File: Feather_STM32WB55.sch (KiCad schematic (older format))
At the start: 45 parts, among them J1 JST-SH Qwiic, J2 Conn_Battery, J3 Conn_ARM_JTAG_SWD_10, J4 Conn_Right, J5 USB_C_Receptacle_USB2.0, J6 Conn_Left, Q1 NTR4171PT1G, SW1 SMD-BUTTON-TOP-DHT-4235A_4P-4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, U1 MCP73831-2-OT, U2 AP2112K-3.3, U3 STM32WB55CGU6, U4 USBLC6-2SC6, U5 Flash SOIC-8, Y1 32Mhz

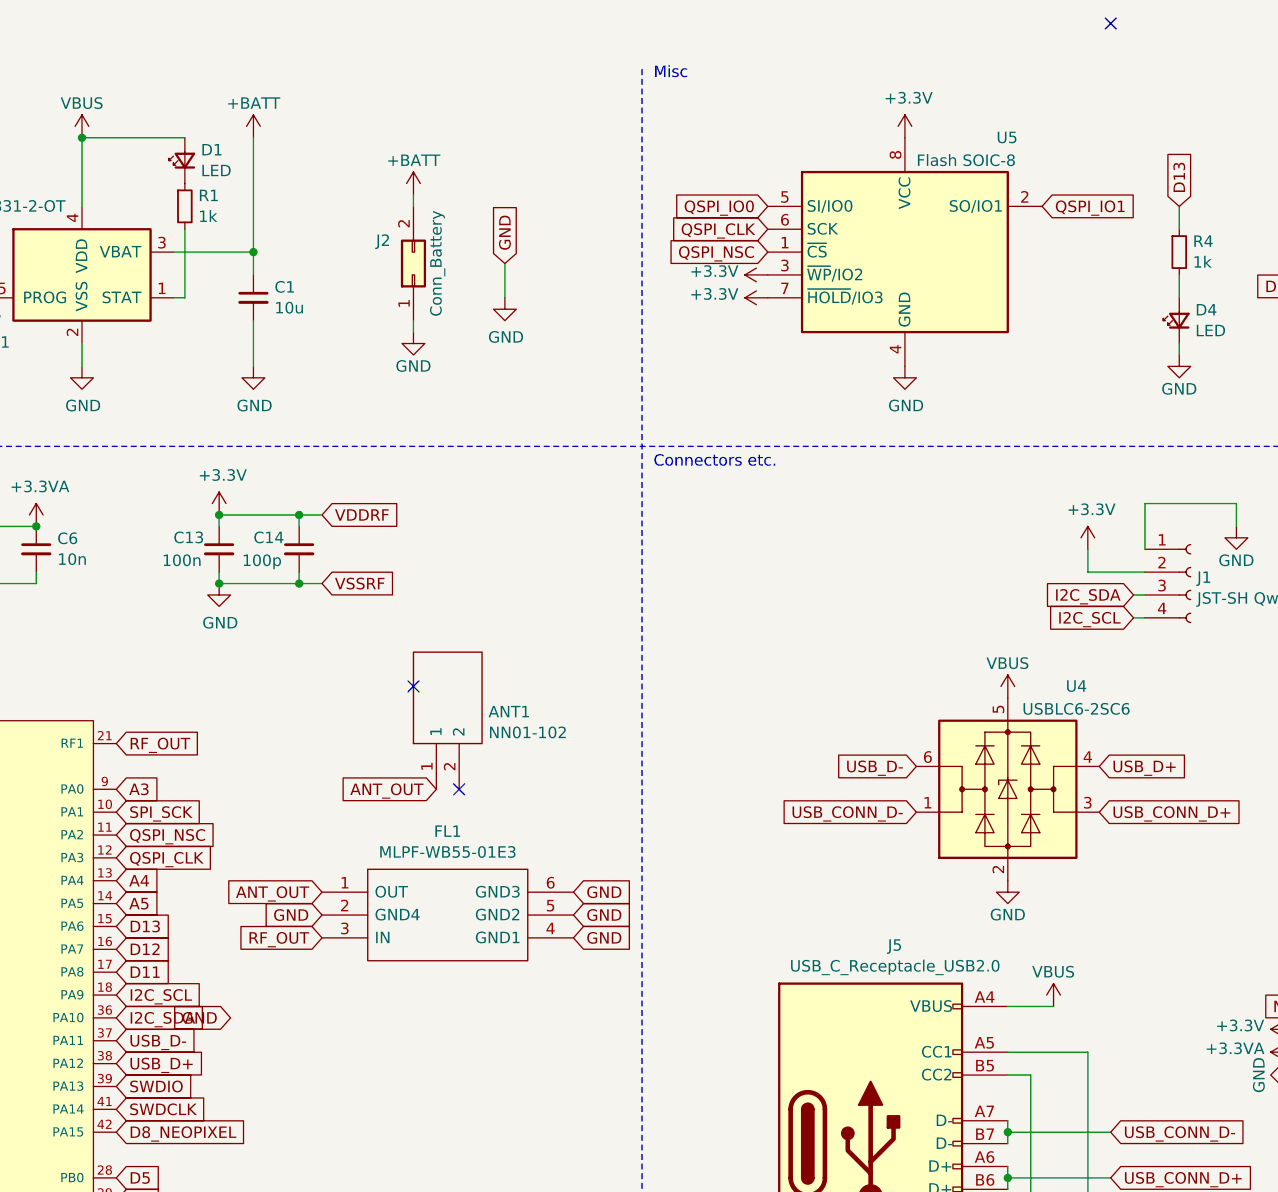
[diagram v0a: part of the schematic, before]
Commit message: fix: repair STM32WB55 short and restore project libraries (#1)
* docs: improve project discovery and reuse guidance

Describe the historical design and available artifacts from repository evidence. Keep hardware and fabrication outputs unchanged, preserve third-party rights, and make unresolved setup and validation limits visible.

* docs: record completed discoverability delivery

* fix: clear the D10 ground short and restore legacy libraries

Move the overlapping ground via using a controlled before/after zone-refilled DRC comparison. Recover original dependencies and align component identifiers without redesigning the land pattern or guessing the physical stackup. Keep historical fabrication outputs explicitly separate from corrected source.

* docs: record completed source audit delivery

* docs: qualify nightly netlist validation by library resolution

Independent export checks show nightly legacy global-library resolution omits the USB shield pin despite identical cached and global pin geometry. Document the exact cache-only invocation and retain the source without speculative wiring changes.
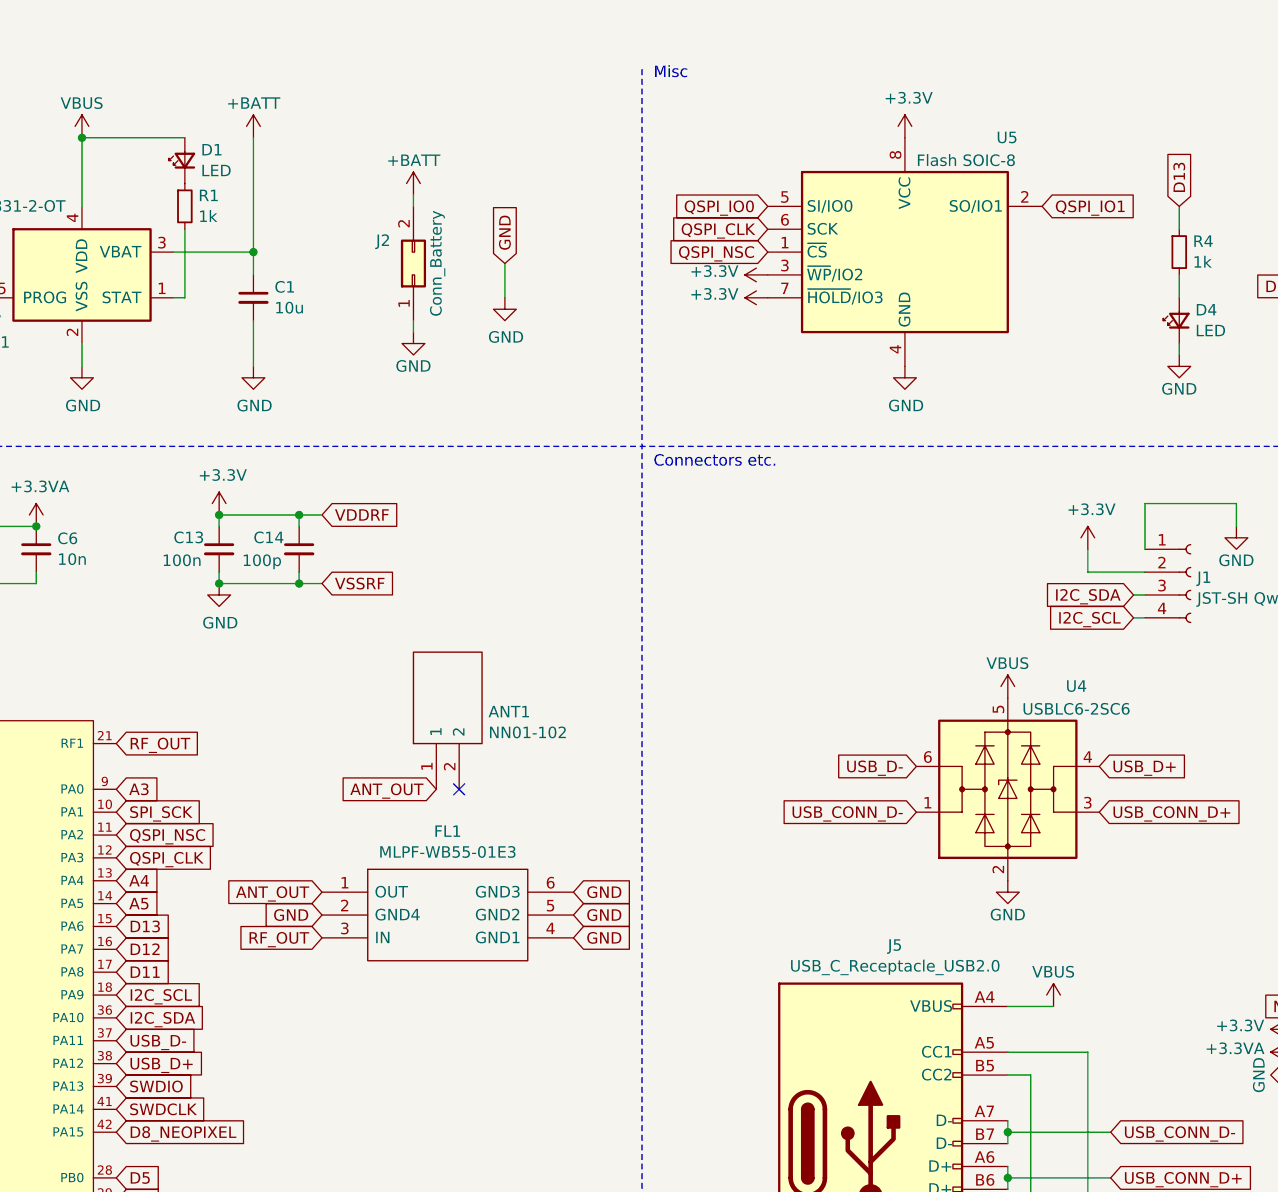
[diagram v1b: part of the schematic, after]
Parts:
- ANT1: footprint FR05S1N0102 -> Makeristic-KiCad-Library:FR05S1N0102
- FL1: footprint MLPFWB5501E3 -> Makeristic-KiCad-Library:MLPFWB5501E3
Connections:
- no-connect marks 10 -> 8
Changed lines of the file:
@@
 Text GLabel 9900 1500 0    50   Input ~ 0
 D8_NEOPIXEL
-NoConn ~ 8700 350
 Text GLabel 9000 1150 1    50   Input ~ 0
 D13
@@
 F 0 "ANT1" V 6088 3472 50  0000 R CNN
 F 1 "NN01-102" V 5997 3472 50  0000 R CNN
-F 2 "FR05S1N0102" H 6400 3800 50  0001 L CNN
+F 2 "Makeristic-KiCad-Library:FR05S1N0102" H 6400 3800 50  0001 L CNN
 F 3 "https://www.fractusantennas.com/files/UM_FR05_S1_N_0_102.pdf" H 6400 3700 50  0001 L CNN
 F 4 "Compact Reach XtendTM (FR05-S1-N-0-102)  Bluetooth, Zigbee, 802.11 b/g/n WLAN" H 6400 3600 50  0001 L CNN "Description"
@@
 	0    -1   -1   0
 $EndComp
-NoConn ~ 5650 3250
 $Comp
 L Makeristic-KiCad-Library:MLPF-WB55-01E3 FL1
@@
 F 0 "FL1" H 5800 4415 50  0000 C CNN
 F 1 "MLPF-WB55-01E3" H 5800 4324 50  0000 C CNN
-F 2 "MLPFWB5501E3" H 6200 4250 50  0001 L CNN
+F 2 "Makeristic-KiCad-Library:MLPFWB5501E3" H 6200 4250 50  0001 L CNN
 F 3 "https://www.st.com/resource/en/datasheet/mlpf-wb55-01e3.pdf" H 6200 4150 50  0001 L CNN
 F 4 "RF Wireless Misc 2.4 GHz Low Pass Filter matched to STM32WB55" H 6200 4050 50  0001 L CNN "Description"
@@
 Text GLabel 6350 4150 2    50   Input ~ 0
 GND
-Text GLabel 4850 4700 0    50   Input ~ 0
-GND
 NoConn ~ 5850 3700
